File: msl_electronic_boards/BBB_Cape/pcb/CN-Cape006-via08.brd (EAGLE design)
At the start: 160 x 86.4 mm, 99 parts, among them IC3 LM340MP-05, IC4 LM2576, IC5 LM2575, P8 BeagleBoard 2x23, P9 BeagleBoard 2x23, U1 ADUM1200ARZ, U2 ADUM1300ARWZ, U3 ADUM1200ARZ, U4 ADUM1300ARWZ

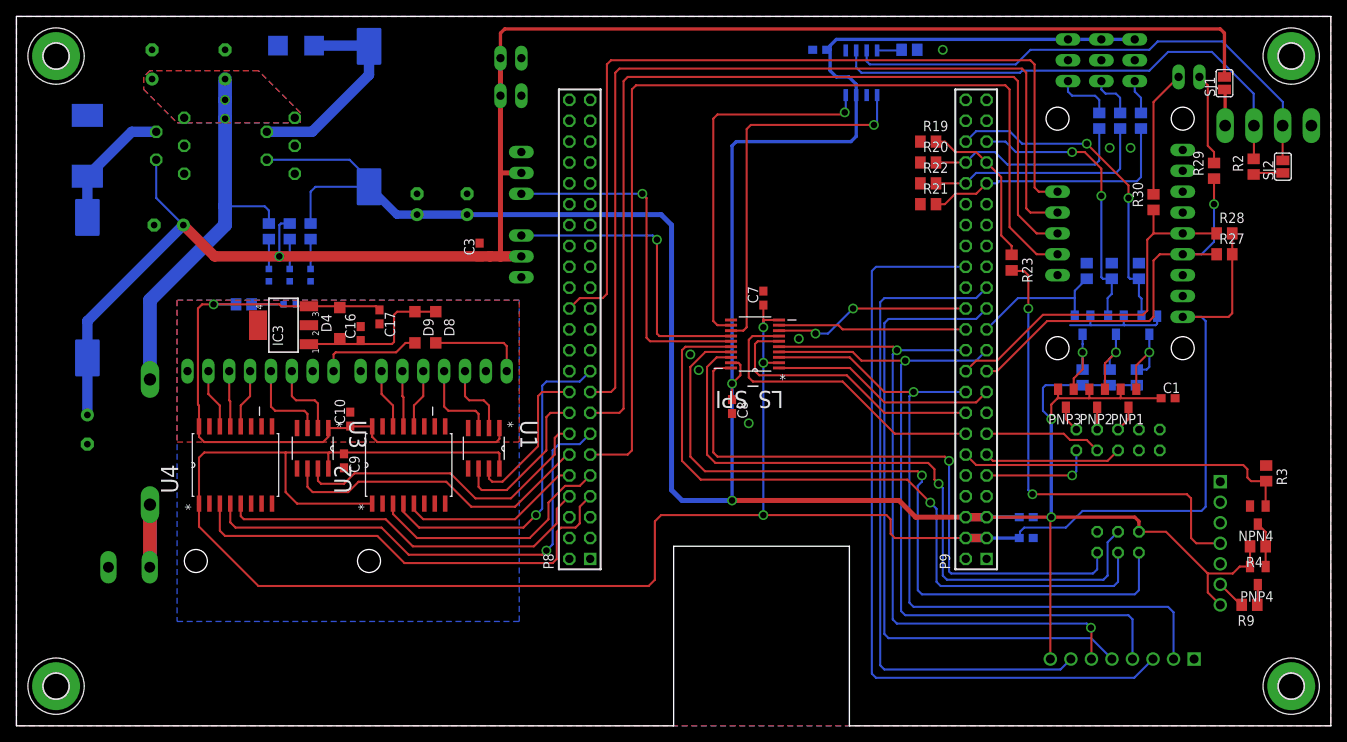
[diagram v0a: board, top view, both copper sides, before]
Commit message: BBB - Task 155 - apply changed conductor tracks
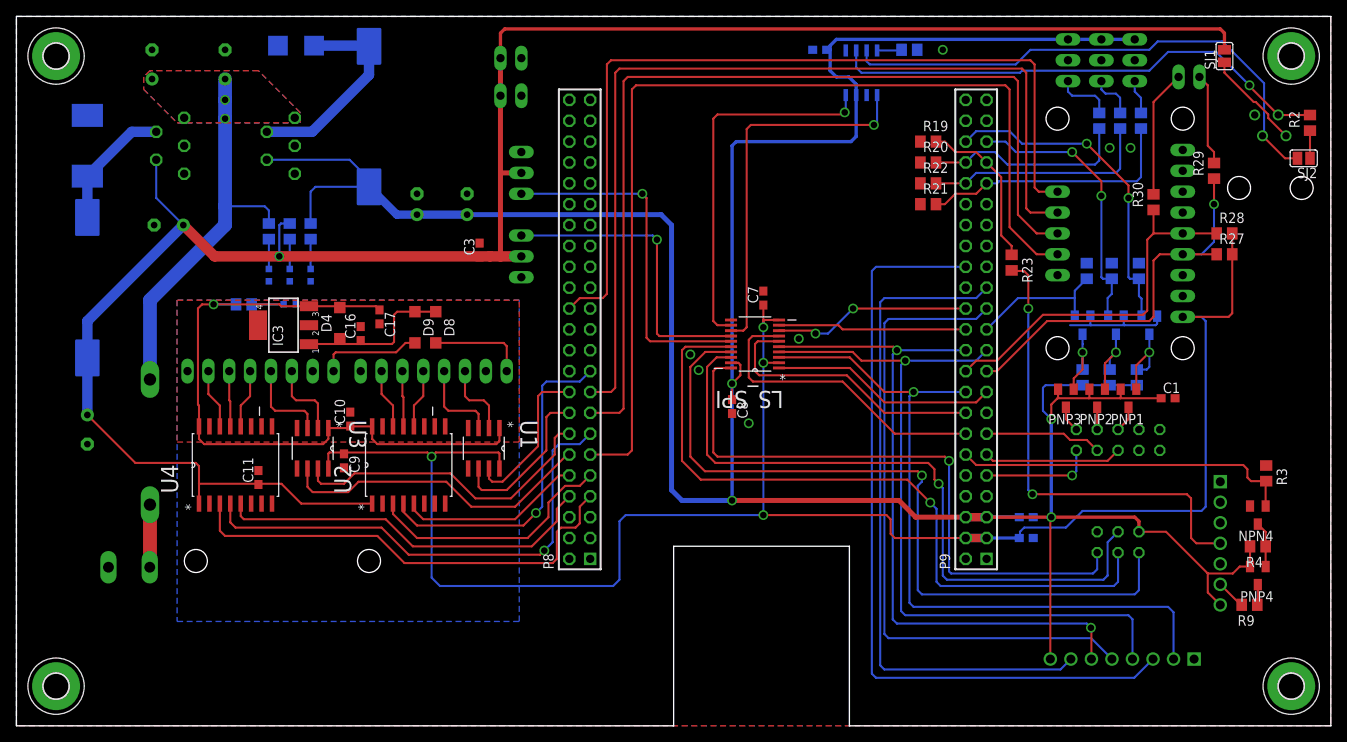
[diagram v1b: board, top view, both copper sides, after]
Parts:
- added C11: 100nF, rcl:C0603
- CAN: value (none) -> RJ10; device con-weidmueller-sl35:90-4 -> ownParts:RJ10
- moved R2 8.69 mm to (157.5, 73.4)
- moved SJ1 3.30 mm to (147.1, 81.5)
- moved SJ2 2.74 mm to (156.7, 69.1), turned to 180 degrees
- moved CAN 2.55 mm to (152.7, 65.3)
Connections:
- removed net 5V/2_F&J: CAN.4, SJ1.1
- new net N$19: CAN.P$1, SJ1.1
- net +3V3: no longer U2.1, U4.1
- net +5V/2: now also C11.1, U2.1, U4.1
- net CANH: now also CAN.P$3; no longer CAN.2
- net CANL: now also CAN.P$2; no longer CAN.3
- net GND: now also C11.2, CAN.P$4; no longer CAN.1
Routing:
- net +3V3: track 277.2 -> 220.8 mm, vias 3 -> 4
- net +5V/2: track 210.1 -> 249.7 mm
- net N$19: track 0.00 -> 12.2 mm
- net 5V/2_F&J: track 4.44 -> 0.00 mm
- net CANH: track 63.5 -> 65.0 mm
- net +5V/3: track 82.4 -> 83.5 mm
- net SW_BUNDLE-LED_3V: track 34.7 -> 33.8 mm
- net CANL: vias 0 -> 1
